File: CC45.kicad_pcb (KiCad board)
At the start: 2 copper layers, 0 parts

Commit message: Placed footprints on pcb and routed everything except the matrix
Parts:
- added C1: 1u, Capacitor_SMD:C_1206_3216Metric_Pad1.42x1.75mm_HandSolder, B.Cu at (161.1, 80.0)
- added C2: 0.1u, Capacitor_SMD:C_1206_3216Metric_Pad1.42x1.75mm_HandSolder, B.Cu at (136.2, 86.6)
- added C3: 0.1u, Capacitor_SMD:C_1206_3216Metric_Pad1.42x1.75mm_HandSolder, B.Cu at (151.3, 95.6)
- added C4: 0.1u, Capacitor_SMD:C_1206_3216Metric_Pad1.42x1.75mm_HandSolder, B.Cu at (147.1, 73.7)
- added C5: 10u, Capacitor_SMD:C_1206_3216Metric_Pad1.42x1.75mm_HandSolder, B.Cu at (154.9, 77.1)
- added C6: 22p, Capacitor_SMD:C_1206_3216Metric_Pad1.42x1.75mm_HandSolder, B.Cu at (137.3, 95.6)
- added C7: 22p, Capacitor_SMD:C_1206_3216Metric_Pad1.42x1.75mm_HandSolder, B.Cu at (148.0, 95.6)
- added D1: D, Diode_SMD:D_SOD-323_HandSoldering, B.Cu at (41.6, 33.2)
- added D10: D, Diode_SMD:D_SOD-323_HandSoldering, B.Cu at (212.6, 33.2)
- added D11: D, Diode_SMD:D_SOD-323_HandSoldering, B.Cu at (231.6, 33.2)
- added D12: D, Diode_SMD:D_SOD-323_HandSoldering, B.Cu at (250.6, 33.2)
- added D13: D, Diode_SMD:D_SOD-323_HandSoldering, B.Cu at (269.6, 33.2)
- added D14: D, Diode_SMD:D_SOD-323_HandSoldering, B.Cu at (43.9, 52.2)
- added D15: D, Diode_SMD:D_SOD-323_HandSoldering, B.Cu at (65.3, 52.2)
- added D16: D, Diode_SMD:D_SOD-323_HandSoldering, B.Cu at (84.3, 52.2)
- added D17: D, Diode_SMD:D_SOD-323_HandSoldering, B.Cu at (103.3, 52.2)
- added D18: D, Diode_SMD:D_SOD-323_HandSoldering, B.Cu at (122.3, 52.2)
- added D19: D, Diode_SMD:D_SOD-323_HandSoldering, B.Cu at (141.3, 52.2)
- added D2: D, Diode_SMD:D_SOD-323_HandSoldering, B.Cu at (60.6, 33.2)
- added D20: D, Diode_SMD:D_SOD-323_HandSoldering, B.Cu at (143.7, 52.2)
- added D21: D, Diode_SMD:D_SOD-323_HandSoldering, B.Cu at (179.3, 52.2)
- added D22: D, Diode_SMD:D_SOD-323_HandSoldering, B.Cu at (198.3, 52.2)
- added D23: D, Diode_SMD:D_SOD-323_HandSoldering, B.Cu at (217.3, 52.2)
- added D24: D, Diode_SMD:D_SOD-323_HandSoldering, B.Cu at (236.3, 52.2)
- added D25: D, Diode_SMD:D_SOD-323_HandSoldering, B.Cu at (262.4, 52.2)
- added D26: D, Diode_SMD:D_SOD-323_HandSoldering, B.Cu at (48.7, 71.2)
- added D27: D, Diode_SMD:D_SOD-323_HandSoldering, B.Cu at (74.8, 71.2)
- added D28: D, Diode_SMD:D_SOD-323_HandSoldering, B.Cu at (93.8, 71.2)
- added D29: D, Diode_SMD:D_SOD-323_HandSoldering, B.Cu at (112.8, 71.2)
- added D3: D, Diode_SMD:D_SOD-323_HandSoldering, B.Cu at (79.6, 33.2)
- added D30: D, Diode_SMD:D_SOD-323_HandSoldering, B.Cu at (131.8, 71.2)
- added D31: D, Diode_SMD:D_SOD-323_HandSoldering, B.Cu at (134.2, 71.2)
- added D32: D, Diode_SMD:D_SOD-323_HandSoldering, B.Cu at (169.8, 71.2)
- added D33: D, Diode_SMD:D_SOD-323_HandSoldering, B.Cu at (188.8, 71.2)
- added D34: D, Diode_SMD:D_SOD-323_HandSoldering, B.Cu at (207.8, 71.2)
- added D35: D, Diode_SMD:D_SOD-323_HandSoldering, B.Cu at (226.8, 71.2)
- added D36: D, Diode_SMD:D_SOD-323_HandSoldering, B.Cu at (245.8, 71.2)
- added D37: D, Diode_SMD:D_SOD-323_HandSoldering, B.Cu at (267.2, 71.2)
- added D38: D, Diode_SMD:D_SOD-323_HandSoldering, B.Cu at (43.9, 90.2)
- added D39: D, Diode_SMD:D_SOD-323_HandSoldering, B.Cu at (65.3, 90.2)
- added D4: D, Diode_SMD:D_SOD-323_HandSoldering, B.Cu at (98.6, 33.2)
- added D40: D, Diode_SMD:D_SOD-323_HandSoldering, B.Cu at (93.2, 90.2)
- added D41: D, Diode_SMD:D_SOD-323_HandSoldering, B.Cu at (110.4, 90.2)
- added D42: D, Diode_SMD:D_SOD-323_HandSoldering, B.Cu at (114.0, 90.2)
- added D43: D, Diode_SMD:D_SOD-323_HandSoldering, B.Cu at (176.9, 90.2)
- added D44: D, Diode_SMD:D_SOD-323_HandSoldering, B.Cu at (200.7, 90.2)
- added D45: D, Diode_SMD:D_SOD-323_HandSoldering, B.Cu at (224.4, 90.2)
- added D46: D, Diode_SMD:D_SOD-323_HandSoldering, B.Cu at (245.8, 90.2)
- added D47: D, Diode_SMD:D_SOD-323_HandSoldering, B.Cu at (267.2, 90.2)
- added D5: D, Diode_SMD:D_SOD-323_HandSoldering, B.Cu at (117.6, 33.2)
- added D6: D, Diode_SMD:D_SOD-323_HandSoldering, B.Cu at (136.6, 33.2)
- added D7: D, Diode_SMD:D_SOD-323_HandSoldering, B.Cu at (138.9, 33.2)
- added D8: D, Diode_SMD:D_SOD-323_HandSoldering, B.Cu at (174.6, 33.2)
- added D9: D, Diode_SMD:D_SOD-323_HandSoldering, B.Cu at (193.6, 33.2)
- added F1: 500m, Fuse:Fuse_1206_3216Metric_Pad1.42x1.75mm_HandSolder, B.Cu at (162.7, 42.8)
- added G***: LOGO, cc:cc, F.Cu at (142.5, 89.1)
- added J1: AVR-ISP-6, random-keyboard-parts:Reset_Pretty-Mask, B.Cu at (173.4, 80.8)
- added R1: 10k, Resistor_SMD:R_1206_3216Metric_Pad1.42x1.75mm_HandSolder, B.Cu at (136.4, 75.3)
- added R2: 22, Resistor_SMD:R_1206_3216Metric_Pad1.42x1.75mm_HandSolder, B.Cu at (150.9, 70.1)
- added R3: 22, Resistor_SMD:R_1206_3216Metric_Pad1.42x1.75mm_HandSolder, B.Cu at (153.8, 70.1)
- added R4: 10k, Resistor_SMD:R_1206_3216Metric_Pad1.42x1.75mm_HandSolder, B.Cu at (153.7, 95.6)
- added R5: 5.1k, Resistor_SMD:R_1206_3216Metric_Pad1.42x1.75mm_HandSolder, B.Cu at (160.3, 36.2)
- added R6: 5.1k, Resistor_SMD:R_1206_3216Metric_Pad1.42x1.75mm_HandSolder, B.Cu at (153.2, 36.2)
- added SW1: RESET, random-keyboard-parts:SKQG-1155865, B.Cu at (163.9, 96.2)
- added SW10: K08, MX_19mm:MX_19mm-1U-NoLED, F.Cu at (185.2, 33.2)
- added SW11: K09, MX_19mm:MX_19mm-1U-NoLED, F.Cu at (204.2, 33.2)
- added SW12: K0A, MX_19mm:MX_19mm-1U-NoLED, F.Cu at (223.2, 33.2)
- added SW13: K0B, MX_19mm:MX_19mm-1U-NoLED, F.Cu at (242.2, 33.2)
- added SW14: K0C, MX_19mm:MX_19mm-1U-NoLED, F.Cu at (261.2, 33.2)
- added SW15: K10, MX_19mm:MX_19mm-1.25U-NoLED, F.Cu at (35.6, 52.2)
- added SW16: K11, MX_19mm:MX_19mm-1U-NoLED, F.Cu at (57.0, 52.2)
- added SW17: K12, MX_19mm:MX_19mm-1U-NoLED, F.Cu at (76.0, 52.2)
- added SW18: K13, MX_19mm:MX_19mm-1U-NoLED, F.Cu at (95.0, 52.2)
- added SW19: K14, MX_19mm:MX_19mm-1U-NoLED, F.Cu at (114.0, 52.2)
- added SW2: K00, MX_19mm:MX_19mm-1U-NoLED, F.Cu at (33.2, 33.2)
- added SW20: K15, MX_19mm:MX_19mm-1U-NoLED, F.Cu at (133.0, 52.2)
- added SW21: K16, MX_19mm:MX_19mm-1U-NoLED, F.Cu at (152.0, 52.2)
- added SW22: K17, MX_19mm:MX_19mm-1U-NoLED, F.Cu at (171.0, 52.2)
- added SW23: K18, MX_19mm:MX_19mm-1U-NoLED, F.Cu at (190.0, 52.2)
- added SW24: K19, MX_19mm:MX_19mm-1U-NoLED, F.Cu at (209.0, 52.2)
- added SW25: K1A, MX_19mm:MX_19mm-1U-NoLED, F.Cu at (228.0, 52.2)
- added SW26: K1B, MX_19mm:MX_19mm-1.75U-NoLED, F.Cu at (254.1, 52.2)
- added SW27: K20, MX_19mm:MX_19mm-1.75U-NoLED, F.Cu at (40.4, 71.2)
- added SW28: K21, MX_19mm:MX_19mm-1U-NoLED, F.Cu at (66.5, 71.2)
- added SW29: K22, MX_19mm:MX_19mm-1U-NoLED, F.Cu at (85.5, 71.2)
- added SW3: K01, MX_19mm:MX_19mm-1U-NoLED, F.Cu at (52.2, 33.2)
- added SW30: K23, MX_19mm:MX_19mm-1U-NoLED, F.Cu at (104.5, 71.2)
- added SW31: K24, MX_19mm:MX_19mm-1U-NoLED, F.Cu at (123.5, 71.2)
- added SW32: K25, MX_19mm:MX_19mm-1U-NoLED, F.Cu at (142.5, 71.2)
- added SW33: K26, MX_19mm:MX_19mm-1U-NoLED, F.Cu at (161.5, 71.2)
- added SW34: K27, MX_19mm:MX_19mm-1U-NoLED, F.Cu at (180.5, 71.2)
- added SW35: K28, MX_19mm:MX_19mm-1U-NoLED, F.Cu at (199.5, 71.2)
- added SW36: K29, MX_19mm:MX_19mm-1U-NoLED, F.Cu at (218.5, 71.2)
- added SW37: K2A, MX_19mm:MX_19mm-1U-NoLED, F.Cu at (237.5, 71.2)
- added SW38: K2B, MX_19mm:MX_19mm-1.25U-NoLED, F.Cu at (258.9, 71.2)
- added SW39: K30, MX_19mm:MX_19mm-1.5U-NoLED, F.Cu at (38.0, 90.2)
- added SW39: K30, MX_19mm:MX_19mm-1.25U-NoLED, F.Cu at (35.6, 90.2)
- added SW4: K02, MX_19mm:MX_19mm-1U-NoLED, F.Cu at (71.2, 33.2)
- added SW40: K31, MX_19mm:MX_19mm-1U-NoLED, F.Cu at (57.0, 90.2)
- added SW41: K32, MX_19mm:MX_19mm-1.5U-NoLED, F.Cu at (85.5, 90.2)
- added SW41: K32, MX_19mm:MX_19mm-1.25U-NoLED, F.Cu at (78.4, 90.2)
- added SW42: K33, MX_19mm:MX_19mm-1.25U-NoLED, F.Cu at (102.1, 90.2)
- added SW43: K34, MX_19mm:MX_19mm-2.25U-ReversedStabilizers-NoLED, F.Cu at (121.1, 90.2)
- added SW43: K34, MX_19mm:MX_19mm-1.75U-NoLED, F.Cu at (130.6, 90.2)
- added SW44: K36, MX_19mm:MX_19mm-6U-ReversedStabilizers-NoLED, F.Cu at (147.2, 90.2)
- added SW44: K36, MX_19mm:MX_19mm-2.75U-ReversedStabilizers-NoLED, F.Cu at (168.6, 90.2)
- added SW44: K36, MX_19mm:MX_19mm-1.75U-NoLED, F.Cu at (163.9, 90.2)
- added SW45: K38, MX_19mm:MX_19mm-1.25U-NoLED, F.Cu at (192.4, 90.2)
- added SW46: K39, MX_19mm:MX_19mm-1.5U-NoLED, F.Cu at (209.0, 90.2)
- added SW46: K39, MX_19mm:MX_19mm-1.25U-NoLED, F.Cu at (216.1, 90.2)
- added SW47: K3A, MX_19mm:MX_19mm-1U-NoLED, F.Cu at (237.5, 90.2)
- added SW48: K3B, MX_19mm:MX_19mm-1.5U-NoLED, F.Cu at (256.5, 90.2)
- added SW48: K3B, MX_19mm:MX_19mm-1.25U-NoLED, F.Cu at (258.9, 90.2)
- added SW5: K03, MX_19mm:MX_19mm-1U-NoLED, F.Cu at (90.2, 33.2)
- added SW6: K04, MX_19mm:MX_19mm-1U-NoLED, F.Cu at (109.2, 33.2)
- added SW7: K05, MX_19mm:MX_19mm-1U-NoLED, F.Cu at (128.2, 33.2)
- added SW8: K06, MX_19mm:MX_19mm-1U-NoLED, F.Cu at (147.2, 33.2)
- added SW9: K07, MX_19mm:MX_19mm-1U-NoLED, F.Cu at (166.2, 33.2)
- added U1: ATmega32U4-AU, Package_QFP:TQFP-44_10x10mm_P0.8mm, B.Cu at (144.5, 81.9)
- added U2: PRTR5V0U2X, random-keyboard-parts:SOT143B, B.Cu at (156.9, 40.4)
- added USB1: HRO-TYPE-C-31-M-12, Type-C:HRO-TYPE-C-31-M-12-HandSoldering, B.Cu at (156.8, 17.8)
- added X1: XTAL, Crystal:Crystal_SMD_3225-4Pin_3.2x2.5mm_HandSoldering, B.Cu at (142.7, 95.6)
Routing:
- net GND: track 0.00 -> 181.6 mm
- net +5V: track 0.00 -> 141.0 mm, vias 0 -> 8
- net /USB_N: track 0.00 -> 52.2 mm
- net /USB_P: track 0.00 -> 52.1 mm
- net RESET: track 0.00 -> 45.4 mm
- net VCC: track 0.00 -> 29.6 mm
- net MOSI: track 0.00 -> 28.7 mm
- net SCK: track 0.00 -> 26.2 mm
- net MISO: track 0.00 -> 23.3 mm, vias 0 -> 1
- net XTAL2: track 0.00 -> 14.6 mm
- net Net-(C1-Pad1): track 0.00 -> 13.0 mm
- net XTAL1: track 0.00 -> 12.2 mm
- net D+: track 0.00 -> 11.2 mm
- net D-: track 0.00 -> 10.4 mm
- net Net-(R5-Pad2): track 0.00 -> 10.3 mm
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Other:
- board outline added: 247 x 80.8 mm
- net class Power added: clearance 0.2, trace_width 0.4, via_dia 0.8, via_drill 0.4

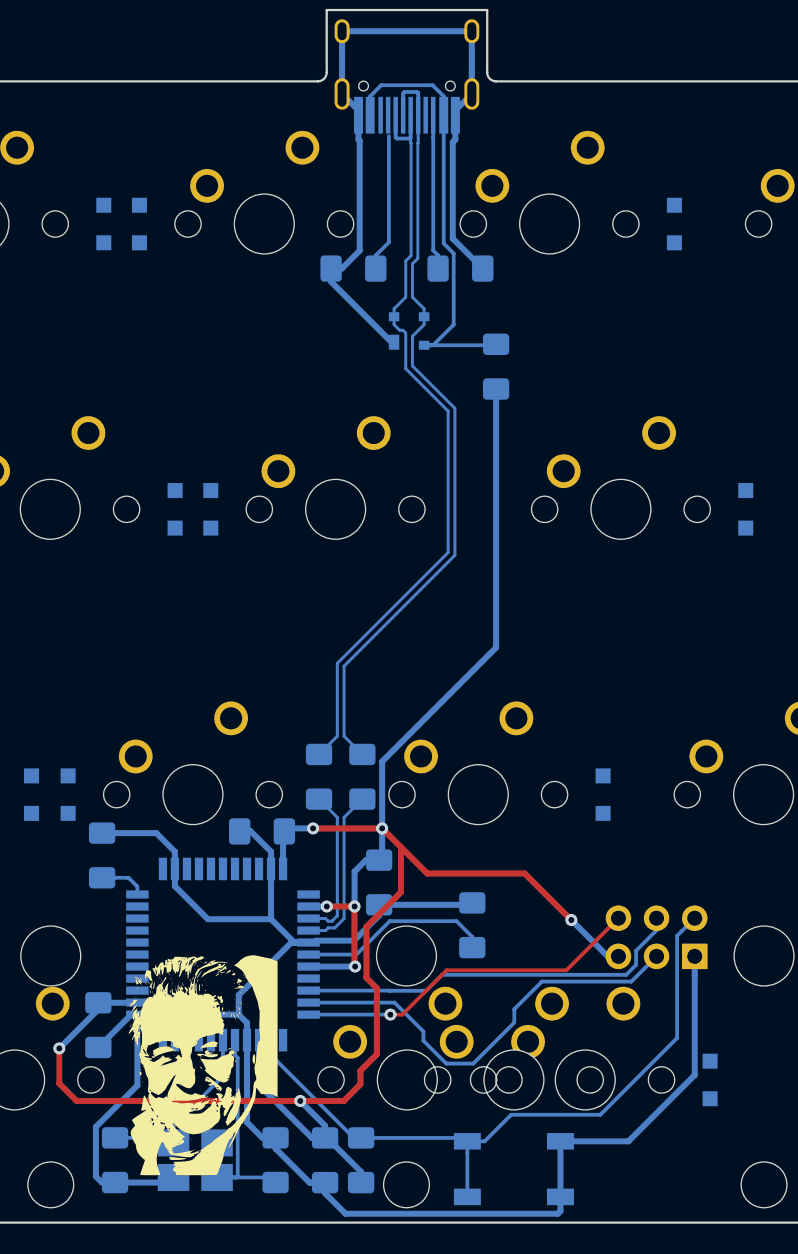
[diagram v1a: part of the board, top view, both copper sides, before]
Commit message: rework components postion around the mcu and usb
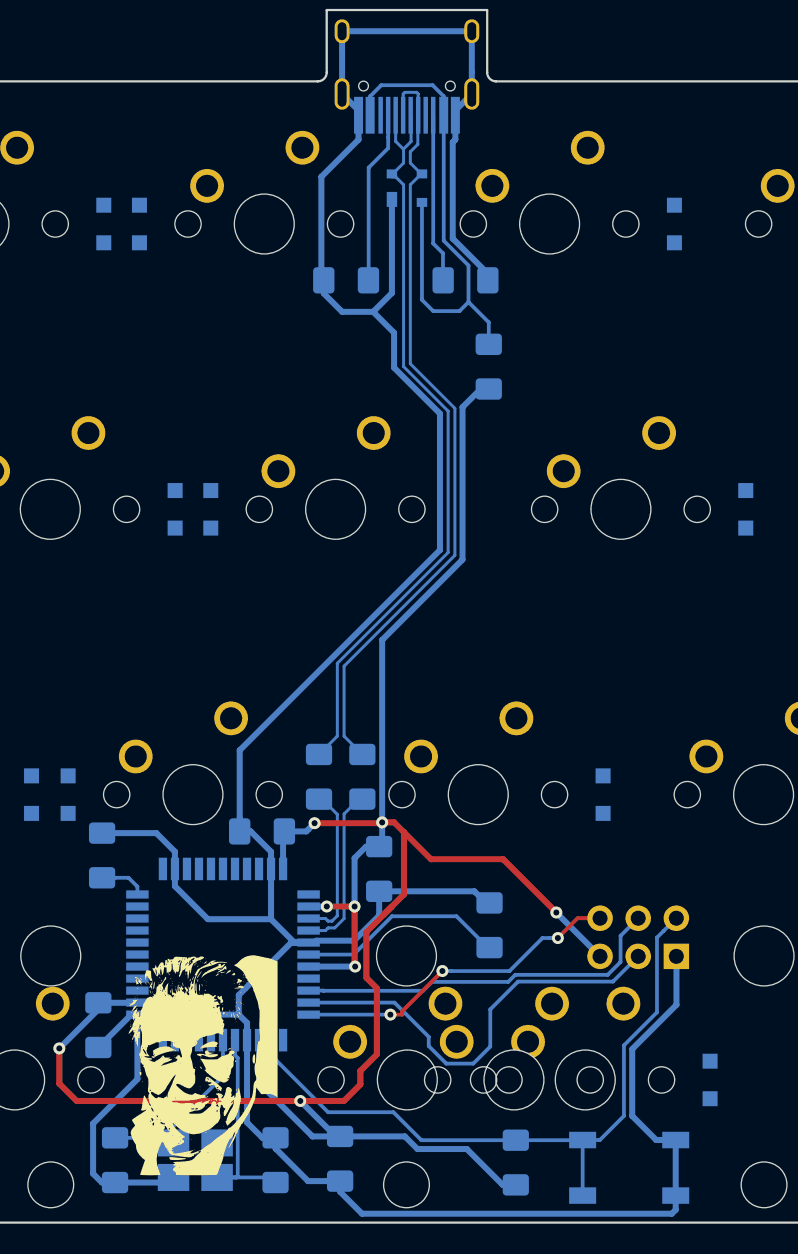
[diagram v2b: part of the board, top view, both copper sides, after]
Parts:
- moved R4 10.3 mm to (164.0, 95.8)
- moved U2 9.51 mm to (156.8, 30.9)
- moved SW1 7.68 mm to (171.6, 96.1)
- moved J1 1.22 mm to (172.2, 80.8)
- moved C1 1.15 mm to (162.2, 80.0)
- moved C3 1.00 mm to (152.3, 95.5)
- moved R6 0.92 mm to (152.7, 37.0)
- moved C5 0.90 mm to (154.9, 76.2)
- moved R5 0.85 mm to (160.7, 37.0)
- moved F1 0.49 mm to (162.2, 42.8)
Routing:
- net GND: track 181.6 -> 236.5 mm
- net +5V: track 141.0 -> 152.5 mm
- net VCC: track 29.6 -> 34.7 mm
- net Net-(R6-Pad2): track 9.18 -> 11.6 mm
- net /USB_N: track 52.2 -> 50.9 mm
- net SCK: track 26.2 -> 25.0 mm
- net MISO: track 23.3 -> 22.2 mm, vias 1 -> 3
- net Net-(C1-Pad1): track 13.0 -> 14.0 mm
- net Net-(R5-Pad2): track 10.3 -> 11.3 mm

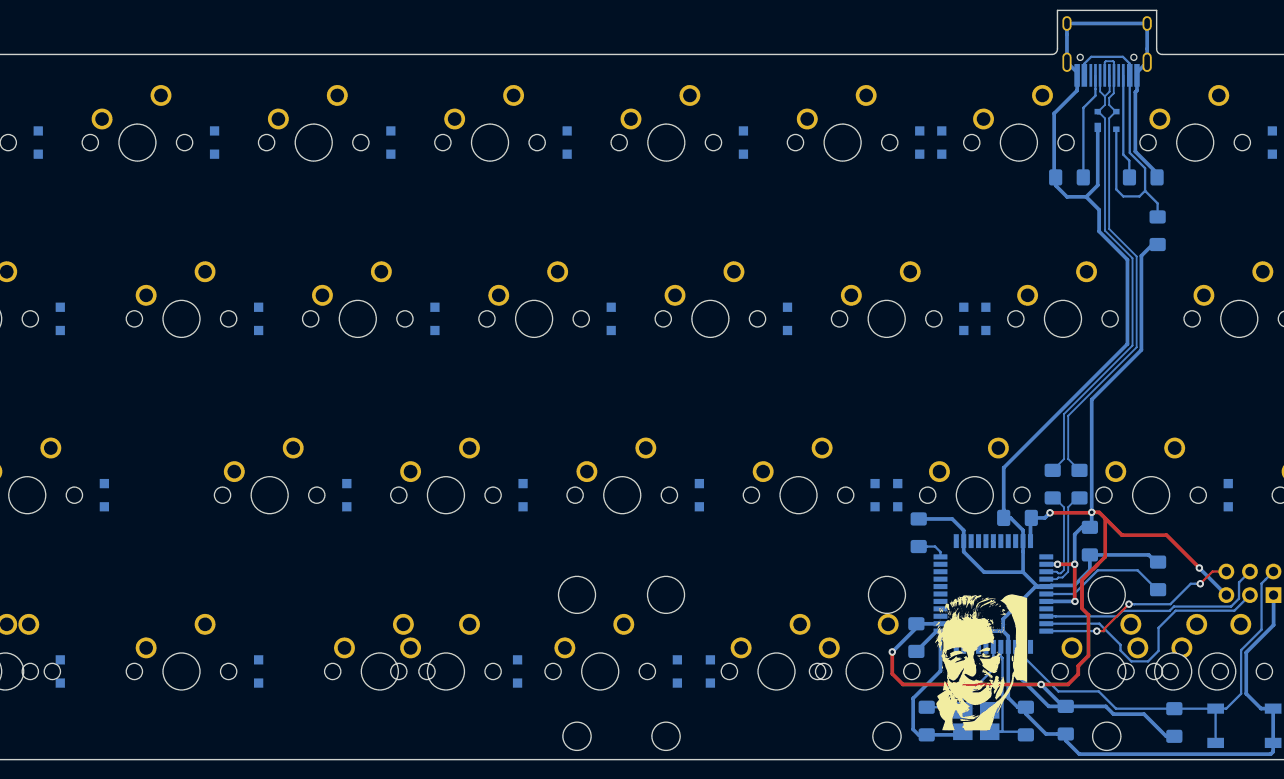
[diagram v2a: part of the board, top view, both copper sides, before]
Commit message: Connect matrix to mcu on the schema and moved some components around
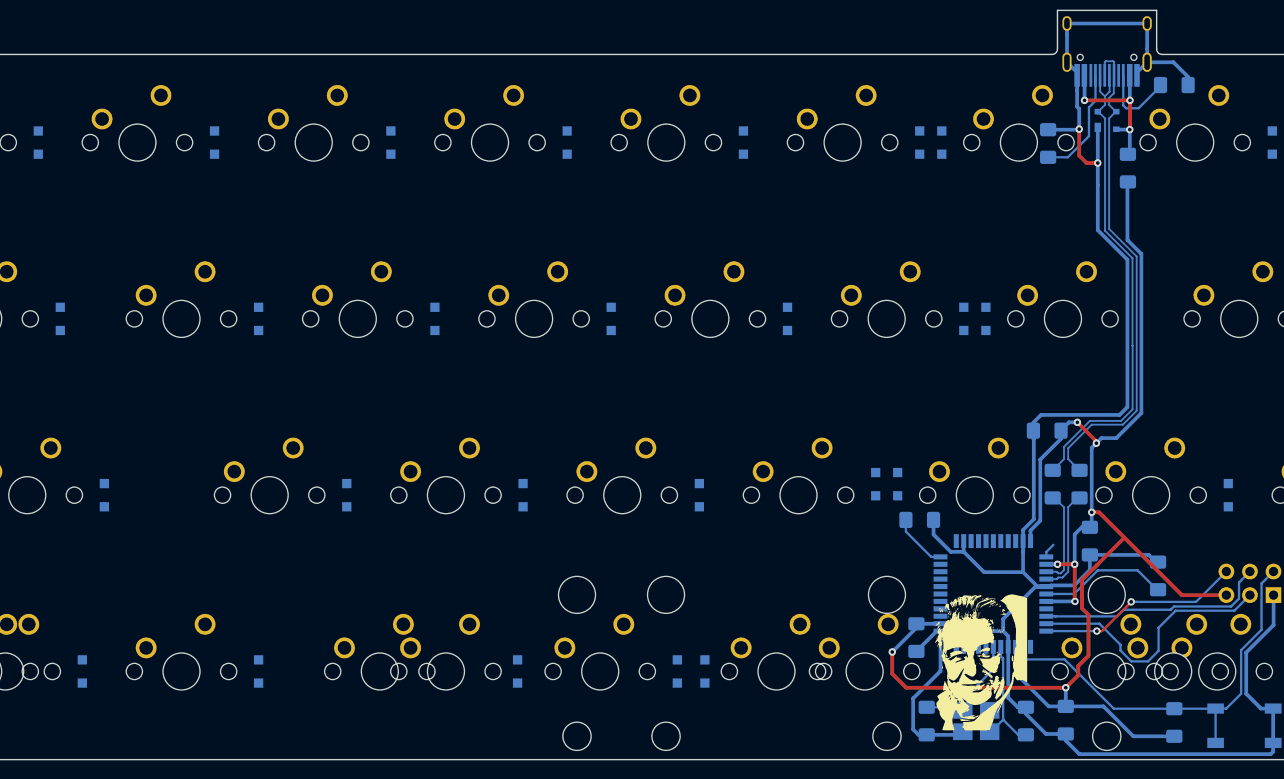
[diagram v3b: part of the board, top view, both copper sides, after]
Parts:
- SW1: value RESET -> SW_Push_Dual
- moved R5 10.5 mm to (164.0, 27.1)
- moved C4 9.93 mm to (150.3, 64.3)
- moved F1 7.47 mm to (159.0, 36.0)
- moved R6 4.31 mm to (150.4, 33.4), turned to -90 degrees
- moved D38 2.38 mm to (46.3, 90.2)
- moved R1 1.39 mm to (136.6, 73.9), turned to 180 degrees
- moved D30 1.19 mm to (131.8, 70.1)
- moved D31 1.19 mm to (134.2, 70.1)
- moved D42 0.59 mm to (113.4, 90.2)
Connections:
- U1 pad 1: Net-(U1-Pad1) -> col7
- U1 pad 12: Net-(U1-Pad12) -> col6
- U1 pad 22: Net-(U1-Pad22) -> row0
- U1 pad 25: Net-(U1-Pad25) -> row3
- U1 pad 26: Net-(U1-Pad26) -> row2
- U1 pad 27: Net-(U1-Pad27) -> row1
- U1 pad 28: Net-(U1-Pad28) -> col0
- U1 pad 29: Net-(U1-Pad29) -> col1
- U1 pad 30: Net-(U1-Pad30) -> col2
- U1 pad 31: Net-(U1-Pad31) -> col3
- U1 pad 32: Net-(U1-Pad32) -> col4
- U1 pad 36: Net-(U1-Pad36) -> col5
- U1 pad 37: Net-(U1-Pad37) -> col8
- U1 pad 38: Net-(U1-Pad38) -> col9
- U1 pad 39: Net-(U1-Pad39) -> col10
- U1 pad 40: Net-(U1-Pad40) -> col11
- U1 pad 41: Net-(U1-Pad41) -> col12
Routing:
- net VCC: track 34.7 -> 17.7 mm, vias 0 -> 3
- net +5V: track 152.5 -> 167.5 mm
- net GND: track 236.5 -> 230.5 mm, vias 0 -> 2
- net Net-(R1-Pad2): track 3.12 -> 6.11 mm
- net Net-(R5-Pad2): track 11.3 -> 8.50 mm
- net /USB_N: track 50.9 -> 52.8 mm
- net /USB_P: track 52.2 -> 54.1 mm
- net col7: track 0.00 -> 1.62 mm
- net XTAL2: track 14.6 -> 13.2 mm
- net Net-(R6-Pad2): track 11.6 -> 12.2 mm
- net MISO: track 22.2 -> 22.1 mm, vias 3 -> 2

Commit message: Routed the matrix
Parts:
- moved C4 1.42 mm to (151.1, 63.1)
- moved C3 1.00 mm to (153.3, 95.5)
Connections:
- U1 pad 22: row0 -> row3
- U1 pad 25: row3 -> row0
- U1 pad 26: row2 -> row1
- U1 pad 27: row1 -> col0
- U1 pad 28: col0 -> row2
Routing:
- net row0: track 0.00 -> 404.0 mm, vias 0 -> 2
- net row1: track 0.00 -> 371.5 mm, vias 0 -> 2
- net row2: track 0.00 -> 344.5 mm, vias 0 -> 2
- net row3: track 0.00 -> 262.2 mm, vias 0 -> 4
- net col11: track 0.00 -> 185.4 mm, vias 0 -> 3
- net col0: track 0.00 -> 168.3 mm, vias 0 -> 1
- net col12: track 0.00 -> 160.6 mm, vias 0 -> 3
- net col10: track 0.00 -> 157.0 mm, vias 0 -> 3
- net col9: track 0.00 -> 147.2 mm, vias 0 -> 3
- net col1: track 0.00 -> 145.6 mm, vias 0 -> 1
- net col2: track 0.00 -> 129.4 mm, vias 0 -> 1
- net col8: track 0.00 -> 128.2 mm, vias 0 -> 3
- net col3: track 0.00 -> 103.9 mm, vias 0 -> 1
- net col4: track 0.00 -> 94.3 mm, vias 0 -> 1
- net col6: track 0.00 -> 84.8 mm, vias 0 -> 5
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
